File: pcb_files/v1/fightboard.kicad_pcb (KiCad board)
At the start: 2 copper layers, 233 x 74 mm, 25 parts, among them J1 SW_Push, K1 SW_Push, M1 XIAO-RP2040, P1 SW_Push, U1 SW_Push, U2 MCP23018-E_SP

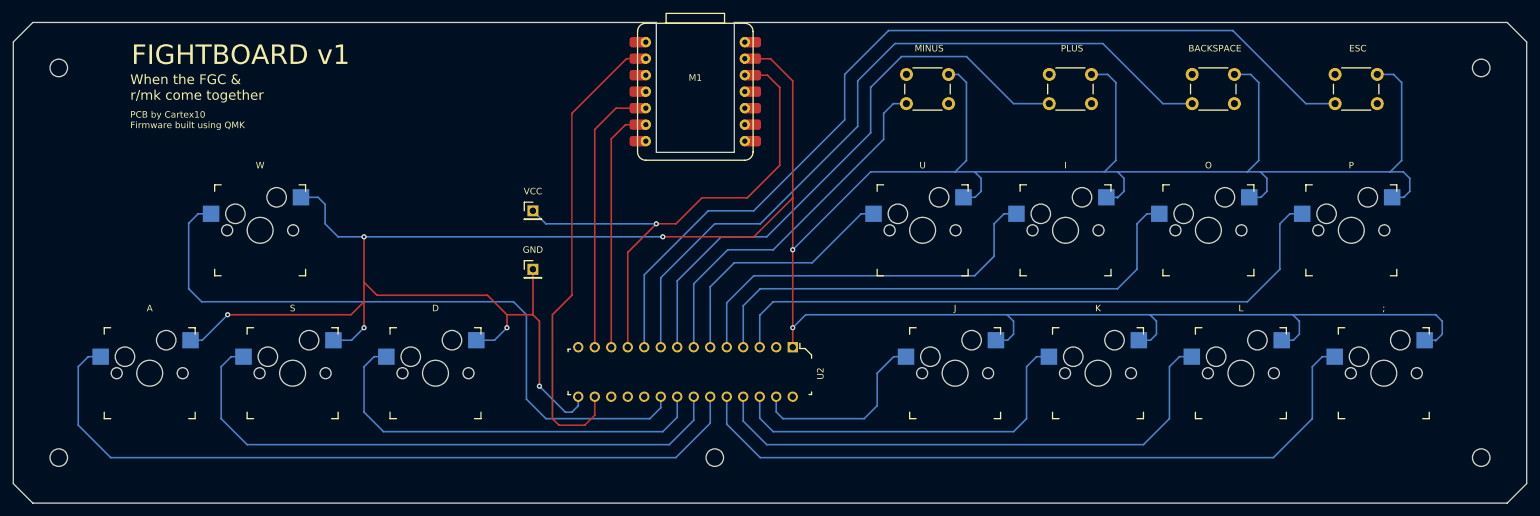
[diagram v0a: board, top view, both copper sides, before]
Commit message: move pcb files into v1 folder
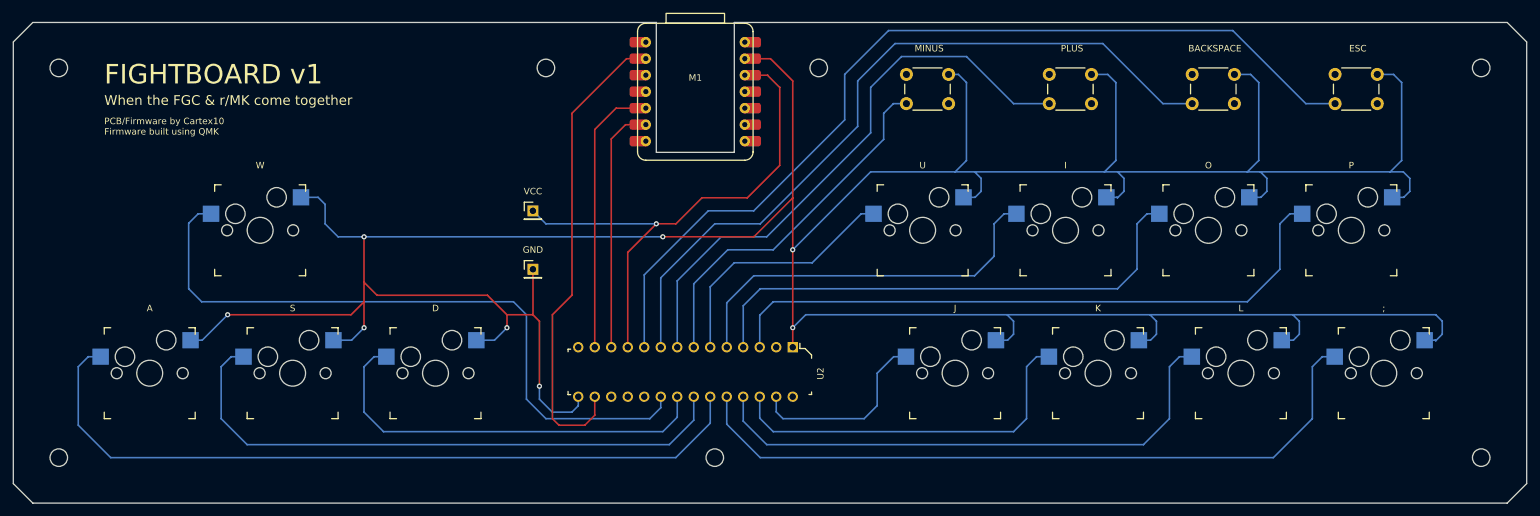
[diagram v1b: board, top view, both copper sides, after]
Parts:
- added REF**: MountingHole_2.7mm, MountingHole:MountingHole_2.7mm, F.Cu at (121.0, 59.0)
- added REF**: MountingHole_2.7mm, MountingHole:MountingHole_2.7mm, F.Cu at (163.0, 59.0)
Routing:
- net Net-(;1-Pad1): track 569.3 -> 570.5 mm
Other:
- board text added: "PCB/Firmware by Cartex10 Firmware built using QMK"
- board text added: "When the FGC & r/MK come together"
- board text removed: "PCB by Cartex10 Firmware built using QMK"
- board text removed: "When the FGC & r/mk come together"
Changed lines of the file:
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@@
       (net 36 "Net-(U2-Pad20)") (pinfunction "2") (pintype "passive"))
+  )
+  (footprint "MountingHole:MountingHole_2.7mm" (layer "F.Cu")
+    (at 121 59)
+    (descr "Mounting Hole 2.7mm, no annular")
+    (tags "mounting hole 2.7mm no annular")
+    (attr exclude_from_pos_files exclude_from_bom)
+    (fp_text reference "REF**" (at 0 -3.7) (layer "Cmts.User")
+      (effects (font (size 1 1) (thickness 0.15)))
+    )
+    (fp_text value "MountingHole_2.7mm" (at 0 3.7) (layer "F.Fab")
+      (effects (font (size 1 1) (thickness 0.15)))
+    )
+    (fp_text user "${REFERENCE}" (at 0 0) (layer "F.Fab")
+      (effects (font (size 1 1) (thickness 0.15)))
+    )
+    (fp_circle (center 0 0) (end 2.7 0) (layer "Cmts.User") (width 0.15) (fill none))
+    (fp_circle (center 0 0) (end 2.95 0) (layer "F.CrtYd") (width 0.05) (fill none))
+    (pad "" np_thru_hole circle (at 0 0) (size 2.7 2.7) (drill 2.7) (layers *.Cu *.Mask))
+  )
+  (footprint "MountingHole:MountingHole_2.7mm" (layer "F.Cu")
+    (at 163 59)
+    (descr "Mounting Hole 2.7mm, no annular")
+    (tags "mounting hole 2.7mm no annular")
+    (attr exclude_from_pos_files exclude_from_bom)
+    (fp_text reference "REF**" (at 0 -3.7) (layer "Cmts.User")
+      (effects (font (size 1 1) (thickness 0.15)))
+    )
+    (fp_text value "MountingHole_2.7mm" (at 0 3.7) (layer "F.Fab")
+      (effects (font (size 1 1) (thickness 0.15)))
+    )
+    (fp_text user "${REFERENCE}" (at 0 0) (layer "F.Fab")
+      (effects (font (size 1 1) (thickness 0.15)))
+    )
+    (fp_circle (center 0 0) (end 2.7 0) (layer "Cmts.User") (width 0.15) (fill none))
+    (fp_circle (center 0 0) (end 2.95 0) (layer "F.CrtYd") (width 0.05) (fill none))
+    (pad "" np_thru_hole circle (at 0 0) (size 2.7 2.7) (drill 2.7) (layers *.Cu *.Mask))
   )
   (footprint "kb_lib:XIAO-RP2040" (layer "F.Cu")
@@
       (effects (font (size 1 1) (thickness 0.15)))
     )
-    (fp_text value "MountingHole_2.7mm" (at 0 3.7) (layer "F.Fab")
+    (fp_text value "MountingHole_2.7mm" (at 0 3.7) (layer "F.Fab") hide
       (effects (font (size 1 1) (thickness 0.15)))
     )
@@
     (effects (font (size 1 1) (thickness 0.15)))
   )
-  (gr_text "FIGHTBOARD v1" (at 74 57) (layer "F.SilkS")
-    (effects (font (size 3 3) (thickness 0.15)))
+  (gr_text "FIGHTBOARD v1" (at 53 60) (layer "F.SilkS")
+    (effects (font (size 3 3) (thickness 0.15)) (justify left))
   )
   (gr_text "GND" (at 119 87) (layer "F.SilkS")
@@
     (effects (font (size 1 1) (thickness 0.15)))
   )
-  (gr_text "When the FGC &\nr/mk come together" (at 57 62) (layer "F.SilkS")
+  (gr_text "When the FGC & r/MK come together" (at 53 64) (layer "F.SilkS")
     (effects (font (size 1.5 1.5) (thickness 0.15)) (justify left))
   )
@@
     (effects (font (size 1 1) (thickness 0.15)))
   )
-  (gr_text "PCB by Cartex10\nFirmware built using QMK" (at 57 67) (layer "F.SilkS")
+  (gr_text "PCB/Firmware by Cartex10\nFirmware built using QMK" (at 53 68) (layer "F.SilkS")
     (effects (font (size 1 1) (thickness 0.15)) (justify left))
   )
@@
   (segment (start 257.92 100.92) (end 258 101) (width 0.25) (layer "B.Cu") (net 31))
   (segment (start 209 79) (end 210 78) (width 0.25) (layer "B.Cu") (net 31))
+  (segment (start 125.98 111.02) (end 125.98 109.62) (width 0.25) (layer "B.Cu") (net 31))
   (segment (start 88.29 100.92) (end 91.08 100.92) (width 0.25) (layer "B.Cu") (net 31))
   (segment (start 231 75) (end 251 75) (width 0.25) (layer "B.Cu") (net 31))
@@
   (segment (start 171 75) (end 159 87) (width 0.25) (layer "B.Cu") (net 31))
   (segment (start 253 75) (end 254 76) (width 0.25) (layer "B.Cu") (net 31))
+  (segment (start 122 112) (end 125 112) (width 0.25) (layer "B.Cu") (net 31))
   (segment (start 91.08 100.92) (end 93 99) (width 0.25) (layer "B.Cu") (net 31))
   (segment (start 215 100) (end 215 98) (width 0.25) (layer "B.Cu") (net 31))
   (segment (start 193 98) (end 192 97) (width 0.25) (layer "B.Cu") (net 31))
-  (segment (start 125 112) (end 124 112) (width 0.25) (layer "B.Cu") (net 31))
   (segment (start 234.29 100.92) (end 236.08 100.92) (width 0.25) (layer "B.Cu") (net 31))
   (segment (start 190.29 100.92) (end 192.08 100.92) (width 0.25) (layer "B.Cu") (net 31))
@@
   (segment (start 207.29 78.92) (end 208.92 78.92) (width 0.25) (layer "B.Cu") (net 31))
   (segment (start 188 76) (end 187 75) (width 0.25) (layer "B.Cu") (net 31))
-  (segment (start 125.98 111.02) (end 125 112) (width 0.25) (layer "B.Cu") (net 31))
   (segment (start 252.75 73.25) (end 252.75 61.25) (width 0.25) (layer "B.Cu") (net 31))
   (segment (start 207 75) (end 208.75 73.25) (width 0.25) (layer "B.Cu") (net 31))
@@
   (segment (start 87 83) (end 87 80) (width 0.25) (layer "B.Cu") (net 31))
   (segment (start 185.75 61.25) (end 184.5 60) (width 0.25) (layer "B.Cu") (net 31))
-  (segment (start 124 112) (end 120 108) (width 0.25) (layer "B.Cu") (net 31))
   (segment (start 207.5 60) (end 205 60) (width 0.25) (layer "B.Cu") (net 31))
   (segment (start 251 75) (end 252.75 73.25) (width 0.25) (layer "B.Cu") (net 31))
@@
   (segment (start 89 85) (end 87 83) (width 0.25) (layer "B.Cu") (net 31))
   (segment (start 161 97) (end 159 99) (width 0.25) (layer "B.Cu") (net 31))
+  (segment (start 125 112) (end 125.98 111.02) (width 0.25) (layer "B.Cu") (net 31))
   (segment (start 161 97) (end 236 97) (width 0.25) (layer "B.Cu") (net 31))
   (segment (start 232 78) (end 232 76) (width 0.25) (layer "B.Cu") (net 31))
@@
   (segment (start 236.08 100.92) (end 237 100) (width 0.25) (layer "B.Cu") (net 31))
   (segment (start 251.5 60) (end 249 60) (width 0.25) (layer "B.Cu") (net 31))
+  (segment (start 120 110) (end 122 112) (width 0.25) (layer "B.Cu") (net 31))
+  (segment (start 120 108) (end 120 110) (width 0.25) (layer "B.Cu") (net 31))
   (segment (start 208.75 61.25) (end 207.5 60) (width 0.25) (layer "B.Cu") (net 31))
   (segment (start 171 75) (end 184 75) (width 0.25) (layer "B.Cu") (net 31))
   (segment (start 214.08 100.92) (end 215 100) (width 0.25) (layer "B.Cu") (net 31))
-  (segment (start 125.98 109.62) (end 125.98 111.02) (width 0.25) (layer "B.Cu") (net 31))
   (segment (start 258 101) (end 259 100) (width 0.25) (layer "B.Cu") (net 31))
   (segment (start 188 78) (end 188 76) (width 0.25) (layer "B.Cu") (net 31))
